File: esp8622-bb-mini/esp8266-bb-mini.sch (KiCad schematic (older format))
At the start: 17 parts, among them J1 Conn_01x02_Male, J2 Conn_01x04_Male, J3 Conn_01x04_Male, J4 Conn_01x04_Male, J5 Conn_01x04_Male, U1 LP38693MP-3.3, U2 ESP-12F

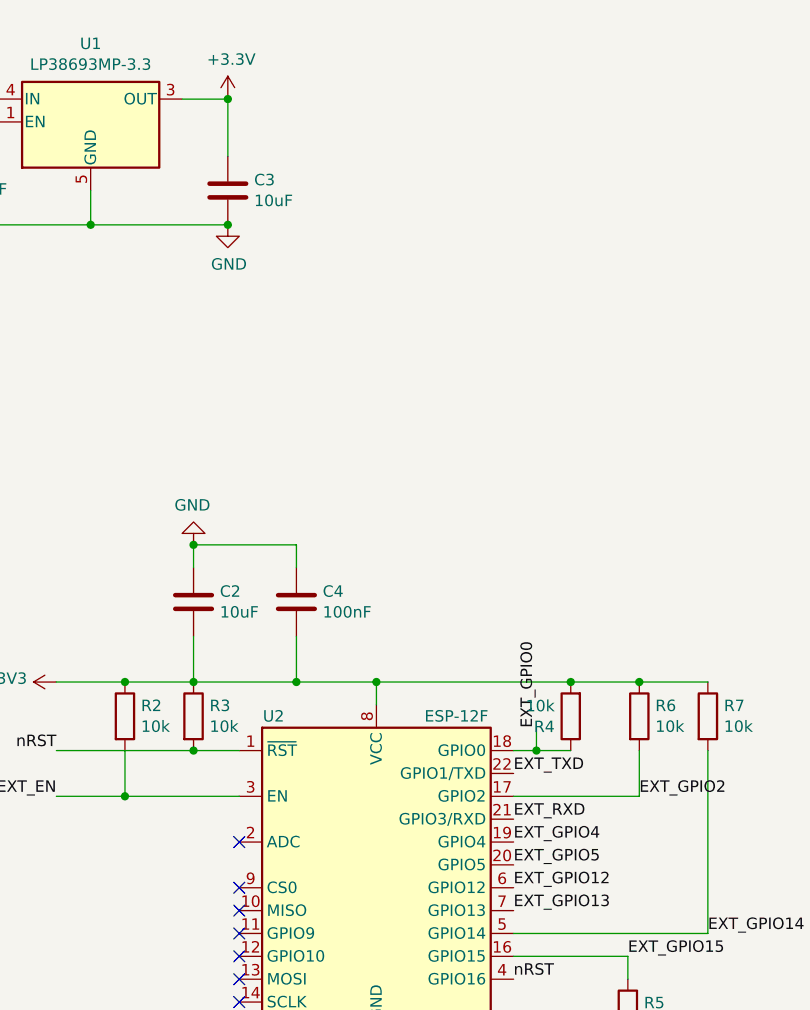
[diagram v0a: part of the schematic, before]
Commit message: sch: add voltage divider for battery level sensing
Signed-off-by: Tillmann Heidsieck <theidsieck@leenox.de>
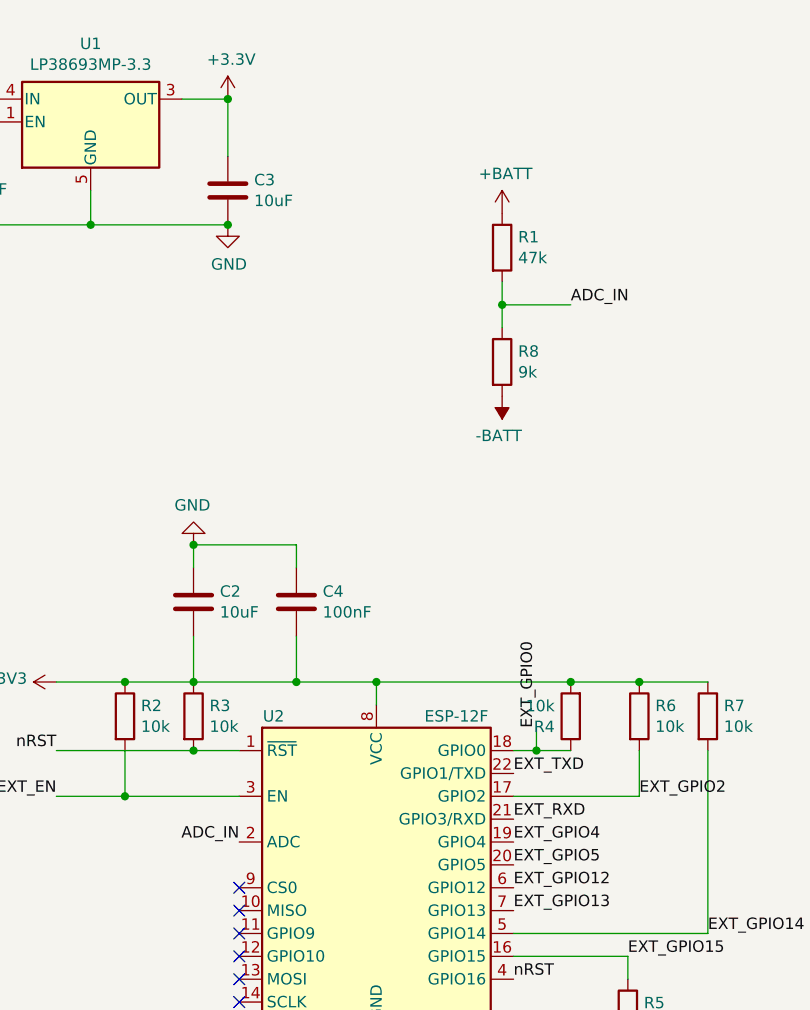
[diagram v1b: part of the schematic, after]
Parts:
- added R1: 47k, Resistor_SMD:R_0402_1005Metric, symbol Device:R
- added R8: 9k, Resistor_SMD:R_0402_1005Metric, symbol Device:R
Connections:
- net +BATT: now also R1.1
- net -BATT: now also R8.2
- net ADC_IN: now reaches U2.2 (ADC)
- net ADC_IN: now also R1.2, R8.1
- no-connect marks 7 -> 6
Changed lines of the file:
@@
 NoConn ~ 3900 5450
 NoConn ~ 3900 5550
-NoConn ~ 3900 4850
 Wire Wire Line
 	3100 4150 3400 4150
@@
 	9000 2250 8700 2250
 Connection ~ 8700 2250
+Text Label 3900 4850 2    50   ~ 0
+ADC_IN
+Text Label 5350 2500 0    50   ~ 0
+ADC_IN
+$Comp
+L power:+BATT #PWR0109
+U 1 1 5FC71883
+P 5050 2100
+F 0 "#PWR0109" H 5050 1950 50  0001 C CNN
+F 1 "+BATT" H 5065 2273 50  0000 C CNN
+F 2 "" H 5050 2100 50  0001 C CNN
+F 3 "" H 5050 2100 50  0001 C CNN
+	1    5050 2100
+	1    0    0    -1
+$EndComp
+$Comp
+L power:-BATT #PWR0110
+U 1 1 5FC72393
+P 5050 2900
+F 0 "#PWR0110" H 5050 2750 50  0001 C CNN
+F 1 "-BATT" H 5065 3073 50  0000 C CNN
+F 2 "" H 5050 2900 50  0001 C CNN
+F 3 "" H 5050 2900 50  0001 C CNN
+	1    5050 2900
+	-1   0    0    1
+$EndComp
+Wire Wire Line
+	5050 2400 5050 2500
+Wire Wire Line
+	5050 2500 5350 2500
+Connection ~ 5050 2500
+Wire Wire Line
+	5050 2500 5050 2600
+$Comp
+L Device:R R8
+U 1 1 5FC6DF52
+P 5050 2750
+F 0 "R8" H 5120 2796 50  0000 L CNN
+F 1 "9k" H 5120 2705 50  0000 L CNN
+F 2 "Resistor_SMD:R_0402_1005Metric" V 4980 2750 50  0001 C CNN
+F 3 "~" H 5050 2750 50  0001 C CNN
+	1    5050 2750
+	1    0    0    -1
+$EndComp
+$Comp
+L Device:R R1
+U 1 1 5FC6F0BF
+P 5050 2250
+F 0 "R1" H 5120 2296 50  0000 L CNN
+F 1 "47k" H 5120 2205 50  0000 L CNN
+F 2 "Resistor_SMD:R_0402_1005Metric" V 4980 2250 50  0001 C CNN
+F 3 "~" H 5050 2250 50  0001 C CNN
+	1    5050 2250
+	1    0    0    -1
+$EndComp
 $EndSCHEMATC
